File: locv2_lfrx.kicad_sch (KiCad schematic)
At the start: 123 parts, among them J2 SMB, T2 Toko CAN1A350EK (5689)

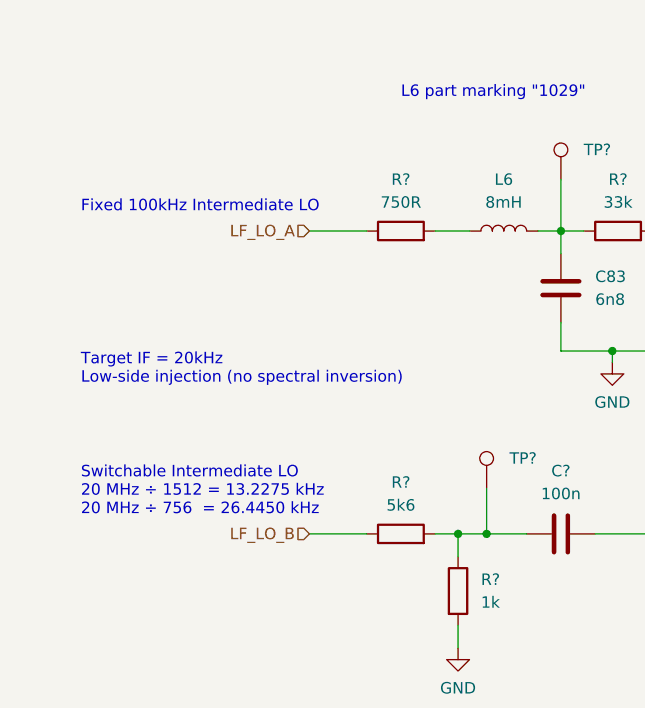
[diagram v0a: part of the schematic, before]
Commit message: Rev B: Fix: Fixed/Variable LO swapped at SA605
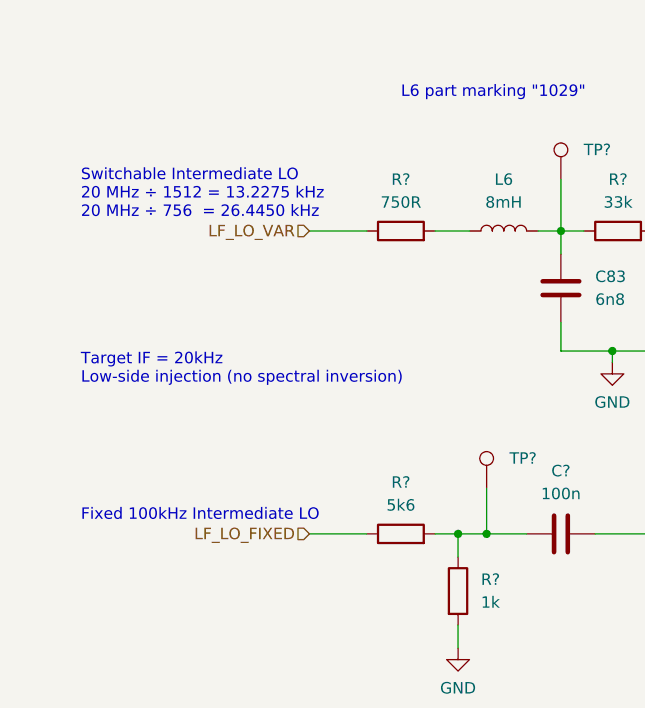
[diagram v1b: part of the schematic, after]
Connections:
- net LF_LO_A renamed LF_LO_VAR
- net LF_LO_B renamed LF_LO_FIXED
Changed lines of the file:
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@@
   (title_block
     (title "Datatrak Locator Mk.2 - LF Nav receiver")
-    (date "2022-06-29")
-    (rev "A")
+    (date "2022-07-08")
+    (rev "B")
   )
   (junction (at 375.285 73.025) (diameter 0) (color 0 0 0 0)
@@
   )
   (text "Switchable Intermediate LO\n20 MHz ÷ 1512 = 13.2275 kHz\n20 MHz ÷ 756  = 26.4450 kHz"
-    (at 25.4 76.835 0)
+    (at 25.4 43.815 0)
     (effects (font (size 1.27 1.27)) (justify left bottom))
   )
@@
     (effects (font (size 1.27 1.27)) (justify left bottom))
   )
-  (text "Fixed 100kHz Intermediate LO" (at 25.4 43.18 0)
+  (text "Fixed 100kHz Intermediate LO" (at 25.4 77.47 0)
     (effects (font (size 1.27 1.27)) (justify left bottom))
   )
@@
     (effects (font (size 1.27 1.27)) (justify left))
   )
-  (hierarchical_label "LF_LO_A" (shape input) (at 50.8 45.085 180)
+  (hierarchical_label "LF_LO_VAR" (shape input) (at 50.8 45.085 180)
     (effects (font (size 1.27 1.27)) (justify right))
   )
@@
     (effects (font (size 1.27 1.27)) (justify left))
   )
-  (hierarchical_label "LF_LO_B" (shape input) (at 50.8 78.74 180)
+  (hierarchical_label "LF_LO_FIXED" (shape input) (at 50.8 78.74 180)
     (effects (font (size 1.27 1.27)) (justify right))
   )
